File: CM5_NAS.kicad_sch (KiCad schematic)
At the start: 14 parts, among them J2 USB_C_Receptacle_USB2.0_14P

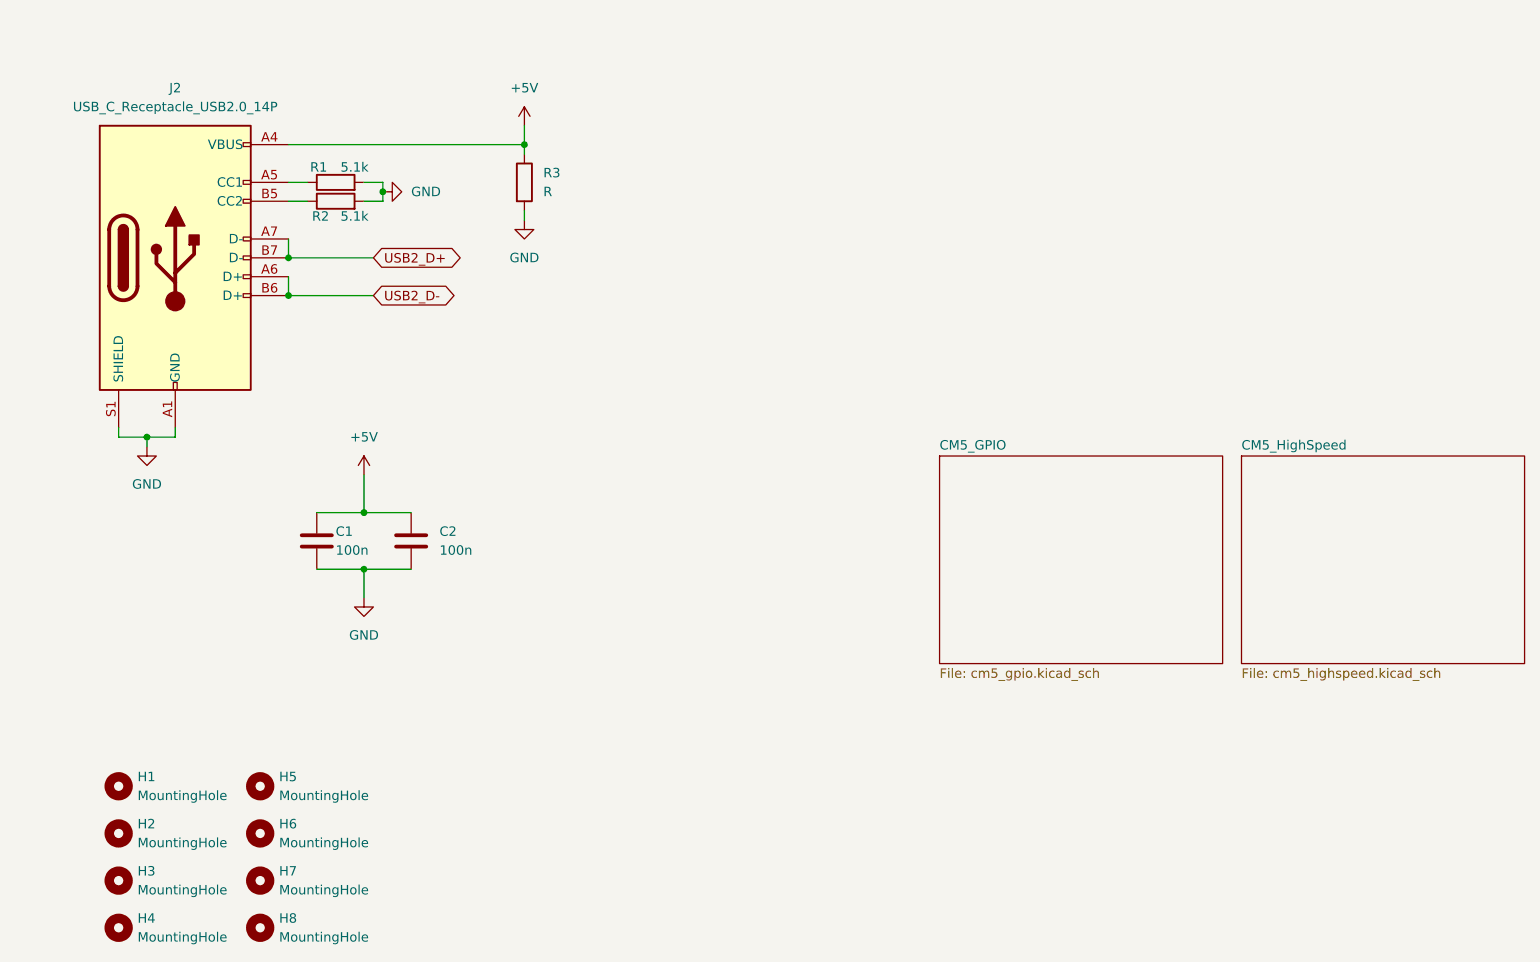
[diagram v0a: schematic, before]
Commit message: create high-speed connects sheet
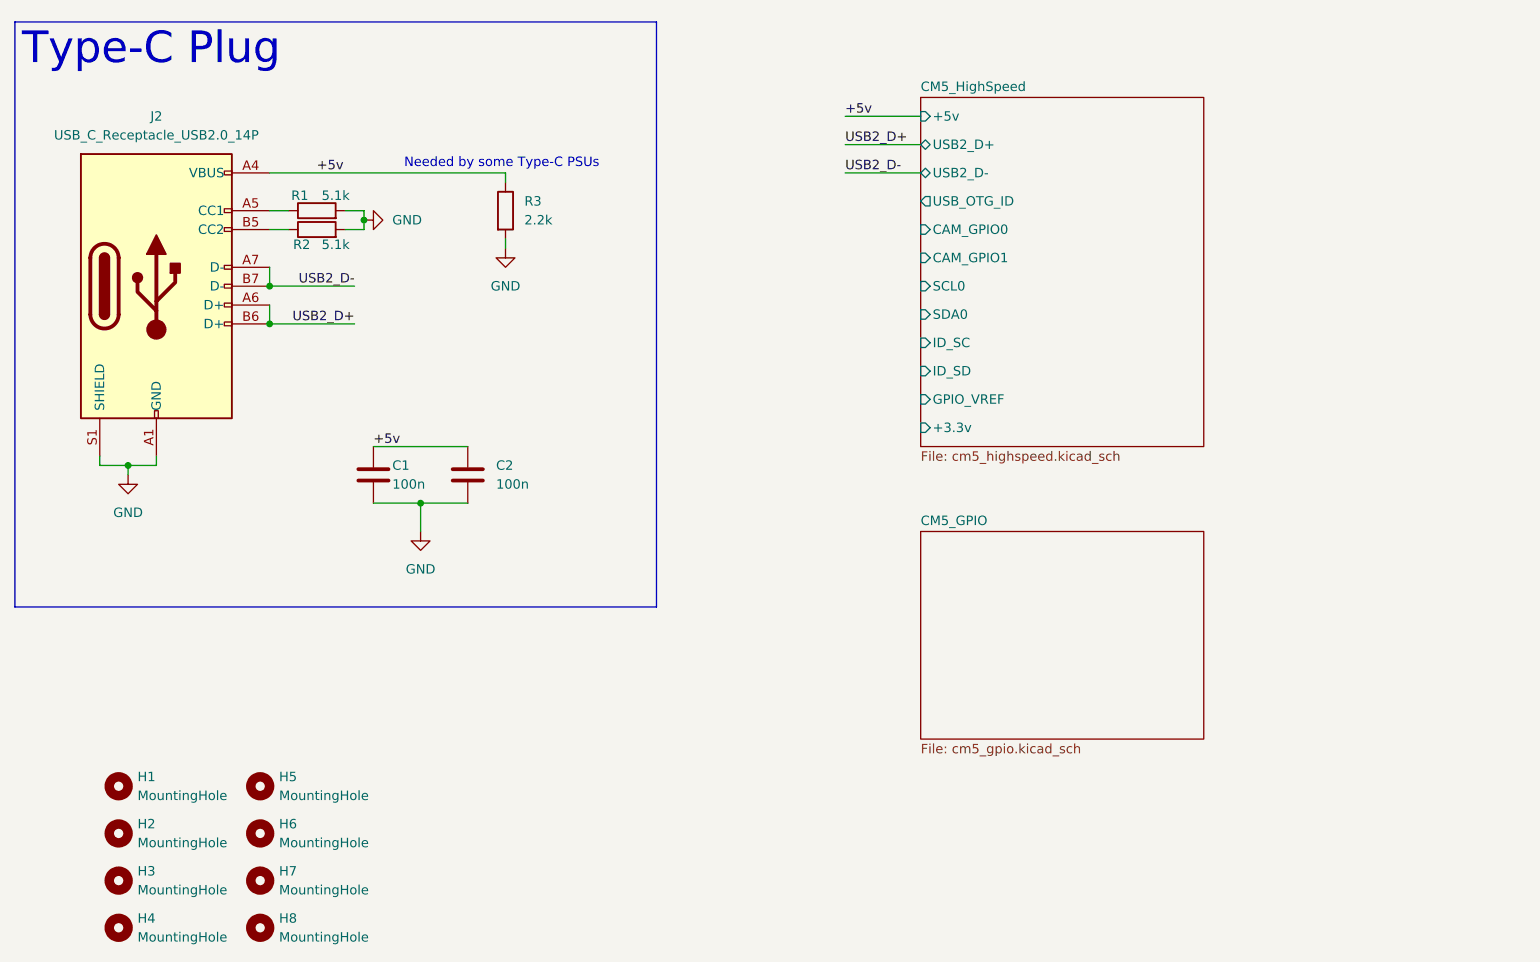
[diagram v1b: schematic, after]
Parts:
- R3: value R -> 2.2k
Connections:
- net USB2_D+: now also J2.A6 (D+), J2.B6 (D+); no longer J2.A7 (D-), J2.B7 (D-)
- net USB2_D-: now also J2.A7 (D-), J2.B7 (D-); no longer J2.A6 (D+), J2.B6 (D+)
- net +5V renamed +5v
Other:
- sheet CM5_HighSpeed ports: added +3.3v, +5v, CAM_GPIO0, CAM_GPIO1, GPIO_VREF, ID_SC, ID_SD, SCL0, SDA0, USB2_D+, USB2_D-, USB_OTG_ID; removed none
- note added: "Needed by some Type-C PSUs"
- moved on the sheet: C1, C2, J2, R1, R2, R3
